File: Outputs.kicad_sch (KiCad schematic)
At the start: 11 parts, among them M2 Module-motor-driver-0.1, M9 Module-motor-driver-0.1, P10 OUT_SPARE_LS2, P12 FP_STATUS, P9 OUT_SPARE_LS1

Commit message: U1 is the library USBLC6-2SC6 (EE-C-0146); J2 part numbers; test pads and proto area out of the BOM
- U1 used the USBLC6-2P6 (SOT-666) symbol with a hand-changed footprint; now EmbeddedEra:USBLC6-2SC6.
- J2 instance had no Manufacturer/MPN although the library has them.
- P1-P32 and G1 are pads, nothing is bought (SOP-008 step 18): in_bom no, as in the library.

Co-Authored-By: Claude Opus 5.5 <noreply@anthropic.com>
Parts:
- P10, P12, P9: now left out of the parts list
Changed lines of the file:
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@@
 		(body_style 1)
 		(exclude_from_sim no)
-		(in_bom yes)
+		(in_bom no)
 		(on_board yes)
 		(in_pos_files yes)
@@
 		(body_style 1)
 		(exclude_from_sim no)
-		(in_bom yes)
+		(in_bom no)
 		(on_board yes)
 		(in_pos_files yes)
@@
 		(body_style 1)
 		(exclude_from_sim no)
-		(in_bom yes)
-		(on_board yes)
-		(in_pos_files yes)
+		(in_bom no)
+		(on_board yes)
+		(in_pos_files yes)

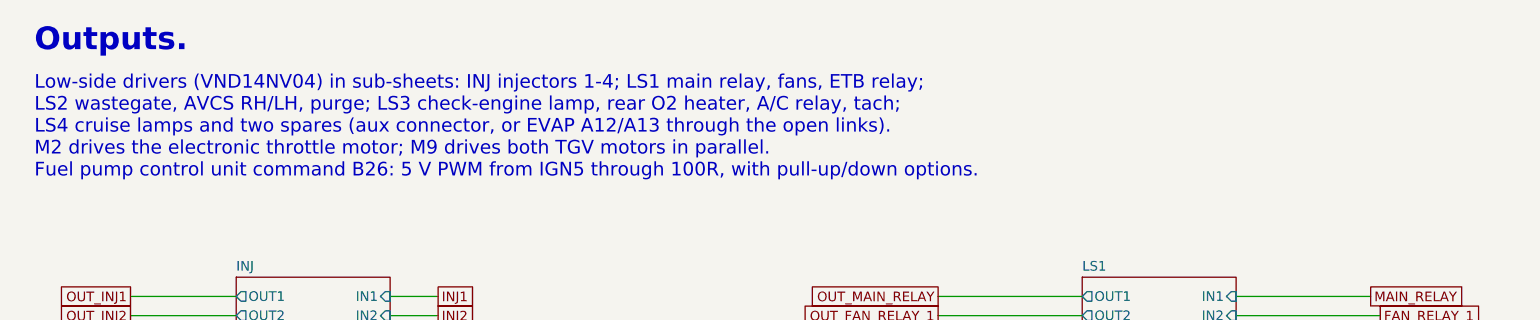
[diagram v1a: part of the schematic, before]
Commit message: Low-side drivers Q1-Q20: VND14NV04-E (obsolete) -> onsemi NCV8401BDTRKG
Same DPAK pinout and TO-252-2 footprint; protected (active clamp, current limit, thermal
shutdown), AEC-Q101, about 28 mOhm at 5 V. Netlist unchanged, 0 overlaps. Schematic PDF
regenerated.

Co-Authored-By: Claude Opus 5.5 <noreply@anthropic.com>
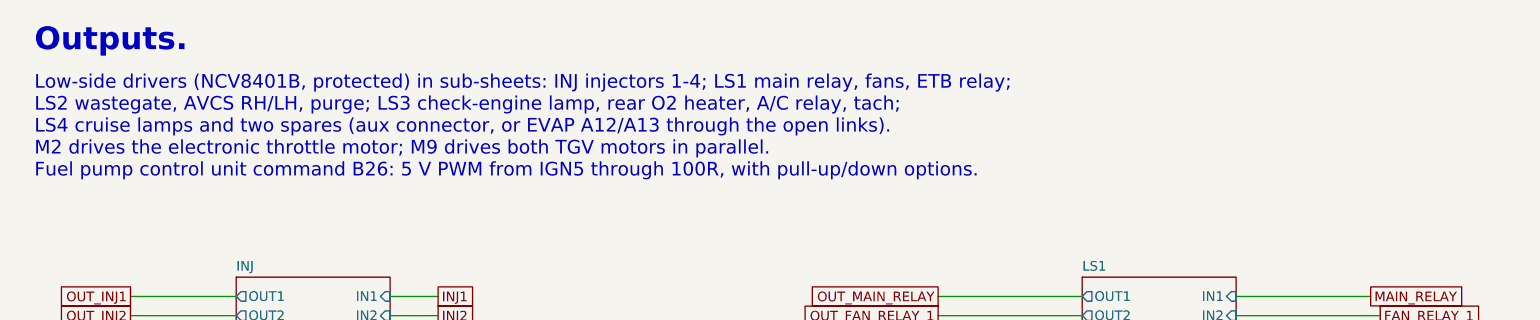
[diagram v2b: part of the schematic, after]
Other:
- note added: "Low-side drivers (NCV8401B, protected) in sub-sheets: INJ injectors 1-4; LS1 main relay, fans, ETB relay; LS2 wastegate, AVCS RH/LH, purge; LS3 check-engine lamp, rear O2 heater, A/C relay, tach; LS4 cruise lamps and two spares (aux connector, or EVAP A12/A13 through the open links). M2 drives the electronic throttle motor; M9 drives both TGV motors in parallel. Fuel pump control unit command B26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"
- note removed: "Low-side drivers (VND14NV04) in sub-sheets: INJ injectors 1-4; LS1 main relay, fans, ETB relay; LS2 wastegate, AVCS RH/LH, purge; LS3 check-engine lamp, rear O2 heater, A/C relay, tach; LS4 cruise lamps and two spares (aux connector, or EVAP A12/A13 through the open links). M2 drives the electronic throttle motor; M9 drives both TGV motors in parallel. Fuel pump control unit command B26: 5 V PWM 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"
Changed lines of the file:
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@@
 		)
 	)
-	(text "Low-side drivers (VND14NV04) in sub-sheets: INJ injectors 1-4; LS1 main relay, fans, ETB relay;\nLS2 wastegate, AVCS RH/LH, purge; LS3 check-engine lamp, rear O2 heater, A/C relay, tach;\nLS4 cruise lamps and two spares (aux connector, or EVAP A12/A13 through the open links).\nM2 drives the electronic throttle motor; M9 drives both TGV motors in parallel.\nFuel pump control unit command B26: 5 V PWM from IGN5 through 100R, with pull-up/down options."
+	(text "Low-side drivers (NCV8401B, protected) in sub-sheets: INJ injectors 1-4; LS1 main relay, fans, ETB relay;\nLS2 wastegate, AVCS RH/LH, purge; LS3 check-engine lamp, rear O2 heater, A/C relay, tach;\nLS4 cruise lamps and two spares (aux connector, or EVAP A12/A13 through the open links).\nM2 drives the electronic throttle motor; M9 drives both TGV motors in parallel.\nFuel pump control unit command B26: 5 V PWM from IGN5 through 100R, with pull-up/down options."
 		(exclude_from_sim no)
 		(at 15.24 22.86 0)

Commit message: Title block: TITLE is the project name (${Project_Name}) on every sheet, DESCRIPTION the sheet name
The LS/INJ sub-sheet and the root had no title at all.

Co-Authored-By: Claude Opus 5.5 <noreply@anthropic.com>
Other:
- title: Outputs -> ${Project_Name}
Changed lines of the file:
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@@
 	(paper "A3")
 	(title_block
-		(title "Outputs")
+		(title "${Project_Name}")
 		(date "2026-10-13")
 	)

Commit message: Low-side drivers sized per load: 8 DPAK (NCV8401B), 4 SOT-223 (ZXMS6006DGQ), 8 SOT-23F (ZXMS6004FF)
INJ and LS2 stay DPAK; LS3 and LS1/LS4 use new sub-sheets with the smaller parts. Purge and the rear
O2 heater swapped groups (LS2/LS3), spares moved to LS3, MIL/tach to LS4; every output keeps its
J1 and MCU pin (checked on the netlist). PCB bank re-placed, planes rebuilt: DRC 0 errors, parity 0.

Co-Authored-By: Claude Opus 5.5 <noreply@anthropic.com>
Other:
- sheet LS1: file INJ4.kicad_sch -> LS_SOT23.kicad_sch
- sheet LS3: file INJ4.kicad_sch -> LS_SOT223.kicad_sch
- sheet LS4: file INJ4.kicad_sch -> LS_SOT23.kicad_sch
- note added: "Protected low-side drivers, sized per load: INJ injectors 1-4 and LS2 wastegate, AVCS RH/LH, rear O2 heater on NCV8401B (DPAK); LS3 purge, A/C relay and the two spares (aux connector, or EVAP A12/A13 through the open links) on ZXMS6006DGQ (SOT-223, 2.8 A); LS1 main relay, fans, ETB relay and LS4 cruise lamps, MIL, tach on ZXMS6004FF (SOT-23F). M2 drives the electronic throttle motor; M9 drives bo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"
- note removed: "Low-side drivers (NCV8401B, protected) in sub-sheets: INJ injectors 1-4; LS1 main relay, fans, ETB relay; LS2 wastegate, AVCS RH/LH, purge; LS3 check-engine lamp, rear O2 heater, A/C relay, tach; LS4 cruise lamps and two spares (aux connector, or EVAP A12/A13 through the open links). M2 drives the electronic throttle motor; M9 drives both TGV motors in parallel. Fuel pump control unit command B26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"
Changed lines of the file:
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@@
 		)
 	)
-	(text "Low-side drivers (NCV8401B, protected) in sub-sheets: INJ injectors 1-4; LS1 main relay, fans, ETB relay;\nLS2 wastegate, AVCS RH/LH, purge; LS3 check-engine lamp, rear O2 heater, A/C relay, tach;\nLS4 cruise lamps and two spares (aux connector, or EVAP A12/A13 through the open links).\nM2 drives the electronic throttle motor; M9 drives both TGV motors in parallel.\nFuel pump control unit command B26: 5 V PWM from IGN5 through 100R, with pull-up/down options."
+	(text "Protected low-side drivers, sized per load: INJ injectors 1-4 and LS2 wastegate, AVCS RH/LH, rear O2 heater on\nNCV8401B (DPAK); LS3 purge, A/C relay and the two spares (aux connector, or EVAP A12/A13 through the open links)\non ZXMS6006DGQ (SOT-223, 2.8 A); LS1 main relay, fans, ETB relay and LS4 cruise lamps, MIL, tach on ZXMS6004FF (SOT-23F).\nM2 drives the electronic throttle motor; M9 drives both TGV motors in parallel.\nFuel pump control unit command B26: 5 V PWM from IGN5 through 100R, with pull-up/down options."
 		(exclude_from_sim no)
 		(at 15.24 22.86 0)
@@
 		)
 	)
-	(global_label "OUT_TACH"
+	(global_label "OUT_SPARE_LS2"
 		(shape passive)
 		(at 346.71 59.69 180)
@@
 		)
 	)
-	(global_label "SPARE_LS1"
+	(global_label "MIL"
 		(shape passive)
 		(at 78.74 80.01 0)
@@
 		)
 	)
-	(global_label "O2_HEATER_REAR"
+	(global_label "AC_RELAY"
 		(shape passive)
 		(at 382.27 54.61 0)
@@
 		)
 	)
-	(global_label "MIL"
+	(global_label "PURGE"
 		(shape passive)
 		(at 382.27 52.07 0)
@@
 		)
 	)
-	(global_label "OUT_O2_HEATER_REAR"
+	(global_label "OUT_AC_RELAY"
 		(shape passive)
 		(at 346.71 54.61 180)
@@
 		)
 	)
-	(global_label "OUT_SPARE_LS2"
+	(global_label "OUT_TACH"
 		(shape passive)
 		(at 43.18 82.55 180)
@@
 		)
 	)
-	(global_label "AC_RELAY"
+	(global_label "SPARE_LS1"
 		(shape passive)
 		(at 382.27 57.15 0)
@@
 		)
 	)
-	(global_label "SPARE_LS2"
+	(global_label "TACH"
 		(shape passive)
 		(at 78.74 82.55 0)
@@
 		)
 	)
-	(global_label "OUT_MIL"
+	(global_label "OUT_PURGE_CONTROL"
 		(shape passive)
 		(at 346.71 52.07 180)
@@
 		)
 	)
-	(global_label "OUT_AC_RELAY"
+	(global_label "OUT_SPARE_LS1"
 		(shape passive)
 		(at 346.71 57.15 180)
@@
 		)
 	)
-	(global_label "TACH"
+	(global_label "SPARE_LS2"
 		(shape passive)
 		(at 382.27 59.69 0)
@@
 		)
 	)
-	(global_label "OUT_SPARE_LS1"
+	(global_label "OUT_MIL"
 		(shape passive)
 		(at 43.18 80.01 180)
@@
 		)
 	)
-	(global_label "PURGE"
+	(global_label "O2_HEATER_REAR"
 		(shape passive)
 		(at 304.8 59.69 0)
@@
 		)
 	)
-	(global_label "OUT_PURGE_CONTROL"
+	(global_label "OUT_O2_HEATER_REAR"
 		(shape passive)
 		(at 269.24 59.69 180)
@@
 			)
 		)
-		(property "Sheetfile" "INJ4.kicad_sch"
+		(property "Sheetfile" "LS_SOT223.kicad_sch"
 			(at 354.33 62.8146 0)
 			(hide yes)
@@
 			)
 		)
-		(property "Sheetfile" "INJ4.kicad_sch"
+		(property "Sheetfile" "LS_SOT23.kicad_sch"
 			(at 50.8 85.6746 0)
 			(hide yes)
@@
 			)
 		)
-		(property "Sheetfile" "INJ4.kicad_sch"
+		(property "Sheetfile" "LS_SOT23.kicad_sch"
 			(at 153.67 62.8146 0)
 			(hide yes)

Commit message: Low-side drivers as on the newest rusEFI boards: 10 x VNLD5160 dual SO-8 + 1 NCV8401B DPAK for the rear O2 heater
rusEFI uaefi-f, hellen-112-17 and hellen154hyundai-e use VNLD5090/VNLD5160 for general outputs and
keep one DPAK for the heaviest load; our Hellen modules already carry their other ICs. Every output
keeps its J1 and MCU pin (netlist checked); U19B parked as a spare. PCB re-placed: DRC 0 errors.

Co-Authored-By: Claude Opus 5.5 <noreply@anthropic.com>
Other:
- sheet INJ: file INJ4.kicad_sch -> LS_VNLD.kicad_sch
- sheet LS1: file LS_SOT23.kicad_sch -> LS_VNLD.kicad_sch
- sheet LS2: file INJ4.kicad_sch -> LS_VNLD.kicad_sch
- sheet LS3: file LS_SOT223.kicad_sch -> LS_MIX.kicad_sch
- sheet LS4: file LS_SOT23.kicad_sch -> LS_VNLD.kicad_sch
- note added: "Protected low-side drivers as on the newest rusEFI boards: dual ST VNLD5160 (SO-8, 2 channels each) for INJ injectors 1-4, LS1 main relay, fans, ETB relay, LS2 wastegate, AVCS RH/LH, purge, LS4 cruise lamps, MIL, tach and LS3 A/C relay and the two spares (aux connector, or EVAP A12/A13 through the open links); the rear O2 heater (~2 A) on one NCV8401B DPAK. M2 drives the electronic throttle motor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"
- note removed: "Protected low-side drivers, sized per load: INJ injectors 1-4 and LS2 wastegate, AVCS RH/LH, rear O2 heater on NCV8401B (DPAK); LS3 purge, A/C relay and the two spares (aux connector, or EVAP A12/A13 through the open links) on ZXMS6006DGQ (SOT-223, 2.8 A); LS1 main relay, fans, ETB relay and LS4 cruise lamps, MIL, tach on ZXMS6004FF (SOT-23F). M2 drives the electronic throttle motor; M9 drives bo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"
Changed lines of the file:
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@@
 		)
 	)
-	(text "Protected low-side drivers, sized per load: INJ injectors 1-4 and LS2 wastegate, AVCS RH/LH, rear O2 heater on\nNCV8401B (DPAK); LS3 purge, A/C relay and the two spares (aux connector, or EVAP A12/A13 through the open links)\non ZXMS6006DGQ (SOT-223, 2.8 A); LS1 main relay, fans, ETB relay and LS4 cruise lamps, MIL, tach on ZXMS6004FF (SOT-23F).\nM2 drives the electronic throttle motor; M9 drives both TGV motors in parallel.\nFuel pump control unit command B26: 5 V PWM from IGN5 through 100R, with pull-up/down options."
+	(text "Protected low-side drivers as on the newest rusEFI boards: dual ST VNLD5160 (SO-8, 2 channels each) for INJ injectors 1-4,\nLS1 main relay, fans, ETB relay, LS2 wastegate, AVCS RH/LH, purge, LS4 cruise lamps, MIL, tach and LS3 A/C relay and the\ntwo spares (aux connector, or EVAP A12/A13 through the open links); the rear O2 heater (~2 A) on one NCV8401B DPAK.\nM2 drives the electronic throttle motor; M9 drives both TGV motors in parallel.\nFuel pump control unit command B26: 5 V PWM from IGN5 through 100R, with pull-up/down options."
 		(exclude_from_sim no)
 		(at 15.24 22.86 0)
@@
 		)
 	)
-	(global_label "OUT_SPARE_LS2"
+	(global_label "OUT_O2_HEATER_REAR"
 		(shape passive)
 		(at 346.71 59.69 180)
@@
 		)
 	)
-	(global_label "AC_RELAY"
+	(global_label "SPARE_LS1"
 		(shape passive)
 		(at 382.27 54.61 0)
@@
 		)
 	)
-	(global_label "PURGE"
+	(global_label "AC_RELAY"
 		(shape passive)
 		(at 382.27 52.07 0)
@@
 		)
 	)
-	(global_label "OUT_AC_RELAY"
+	(global_label "OUT_SPARE_LS1"
 		(shape passive)
 		(at 346.71 54.61 180)
@@
 		)
 	)
-	(global_label "SPARE_LS1"
+	(global_label "SPARE_LS2"
 		(shape passive)
 		(at 382.27 57.15 0)
@@
 		)
 	)
-	(global_label "OUT_PURGE_CONTROL"
+	(global_label "OUT_AC_RELAY"
 		(shape passive)
 		(at 346.71 52.07 180)
@@
 		)
 	)
-	(global_label "OUT_SPARE_LS1"
+	(global_label "OUT_SPARE_LS2"
 		(shape passive)
 		(at 346.71 57.15 180)
@@
 		)
 	)
-	(global_label "SPARE_LS2"
+	(global_label "O2_HEATER_REAR"
 		(shape passive)
 		(at 382.27 59.69 0)
@@
 		)
 	)
-	(global_label "O2_HEATER_REAR"
+	(global_label "PURGE"
 		(shape passive)
 		(at 304.8 59.69 0)
@@
 		)
 	)
-	(global_label "OUT_O2_HEATER_REAR"
+	(global_label "OUT_PURGE_CONTROL"
 		(shape passive)
 		(at 269.24 59.69 180)
@@
 			)
 		)
-		(property "Sheetfile" "LS_SOT223.kicad_sch"
+		(property "Sheetfile" "LS_MIX.kicad_sch"
 			(at 354.33 62.8146 0)
 			(hide yes)
@@
 			)
 		)
-		(property "Sheetfile" "INJ4.kicad_sch"
+		(property "Sheetfile" "LS_VNLD.kicad_sch"
 			(at 41.91 62.8146 0)
 			(hide yes)
@@
 			)
 		)
-		(property "Sheetfile" "INJ4.kicad_sch"
+		(property "Sheetfile" "LS_VNLD.kicad_sch"
 			(at 276.86 62.8146 0)
 			(hide yes)
@@
 			)
 		)
-		(property "Sheetfile" "LS_SOT23.kicad_sch"
+		(property "Sheetfile" "LS_VNLD.kicad_sch"
 			(at 50.8 85.6746 0)
 			(hide yes)
@@
 			)
 		)
-		(property "Sheetfile" "LS_SOT23.kicad_sch"
+		(property "Sheetfile" "LS_VNLD.kicad_sch"
 			(at 153.67 62.8146 0)
 			(hide yes)
